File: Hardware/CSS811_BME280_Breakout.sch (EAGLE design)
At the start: 30 parts, among them J1 GATORGATOR_MINI, J2 GATORGATOR_MINI, J3 GATORGATOR_MINI, J4 GATORGATOR_MINI, J5 GATORGATOR_MINI, J6 GATORGATOR_MINI, J7 GATORGATOR_MINI, J8 GATORGATOR_MINI, U2 CCS811, U3 BME280

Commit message: resizing board, adding silk
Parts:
- added LOGO2: SFE_LOGO_NAME_FLAME.1_INCH, SparkFun-Aesthetics:SFE_LOGO_NAME_FLAME.1_INCH
- LOGO1: value SFE_LOGO_NAME.1_INCH -> SFE_LOGO_NAME_FLAME.1_INCH; device SparkFun-Aesthetics:SFE_LOGO_NAME.1_INCH -> SparkFun-Aesthetics:SFE_LOGO_NAME_FLAME.1_INCH
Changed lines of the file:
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@@
 <part name="GND1" library="SparkFun-PowerSymbols" deviceset="GND" device=""/>
 <part name="SUPPLY4" library="SparkFun-PowerSymbols" deviceset="3.3V" device=""/>
-<part name="LOGO1" library="SparkFun-Aesthetics" deviceset="SFE_LOGO_NAME" device=".1_INCH"/>
+<part name="LOGO1" library="SparkFun-Aesthetics" deviceset="SFE_LOGO_NAME_FLAME" device=".1_INCH"/>
 <part name="FD3" library="SparkFun-Aesthetics" deviceset="FIDUCIAL" device="1X2"/>
 <part name="FD4" library="SparkFun-Aesthetics" deviceset="FIDUCIAL" device="1X2"/>
@@
 <part name="J7" library="SparkFun-Connectors" deviceset="GATOR" device="GATOR_MINI"/>
 <part name="J8" library="SparkFun-Connectors" deviceset="GATOR" device="GATOR_MINI"/>
+<part name="LOGO2" library="SparkFun-Aesthetics" deviceset="SFE_LOGO_NAME_FLAME" device=".1_INCH"/>
 </parts>
 <sheets>
@@
 <attribute name="VALUE" x="109.22" y="68.834" size="1.778" layer="96" font="vector" rot="MR0" align="bottom-center"/>
 </instance>
-<instance part="LOGO1" gate="G$1" x="88.9" y="2.54" smashed="yes"/>
+<instance part="LOGO1" gate="G$1" x="91.44" y="2.54" smashed="yes"/>
 <instance part="FD3" gate="G$1" x="241.3" y="27.94" smashed="yes"/>
 <instance part="FD4" gate="G$1" x="241.3" y="25.4" smashed="yes"/>
@@
 <attribute name="NAME" x="119.38" y="60.96" size="1.778" layer="95" font="vector"/>
 </instance>
+<instance part="LOGO2" gate="G$1" x="91.44" y="2.54" smashed="yes"/>
 </instances>
 <busses>

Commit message: finalizing layout/silk
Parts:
- removed ADR1, ADR2: JUMPER-SMT_2_NO_SILK, SparkFun-Jumpers:JUMPER-SMT_2_NO_SILK
- removed JP1: JUMPER-SMT_3_2-NC_TRACE_SILK, SparkFun-Jumpers:JUMPER-SMT_3_2-NC_TRACE_SILK
- LOGO1: value SFE_LOGO_NAME_FLAME.1_INCH -> SFE_LOGO_NAME.1_INCH; device SparkFun-Aesthetics:SFE_LOGO_NAME_FLAME.1_INCH -> SparkFun-Aesthetics:SFE_LOGO_NAME.1_INCH
- R13, R14: value 4.7k -> 10k; device SparkFun-Resistors:4.7KOHM-0603-1/10W-1% -> SparkFun-Resistors:10KOHM-0603-1/10W-1%
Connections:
- removed net N$4: JP1.3, R13.2
- removed net N$5: JP1.1, R14.2
- net 3.3V: now also R13.2, R14.2; no longer JP1.2
- net CCS811_ADDR: no longer ADR1.2
- net GND: no longer ADR1.1, ADR2.1
- net SDO/ADR: no longer ADR2.2
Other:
- note added: "The I2C address of the BME280 is fixed at 0x77"
- note added: "The address of the CCS811 is 0x5B"
- note removed: "ADR1 sets the I2C address of the CCS811. Open (Default) - 0x5B Closed - 0x5A"
- note removed: "ADR2 sets the I2C address of the BME280. Open (Default) - 0x77 Closed - 0x76"
- note removed: "BME280 is configured to I2C mode"
- note removed: "JP1 connects SDA and SCL to 4.7k pull-up resistors."

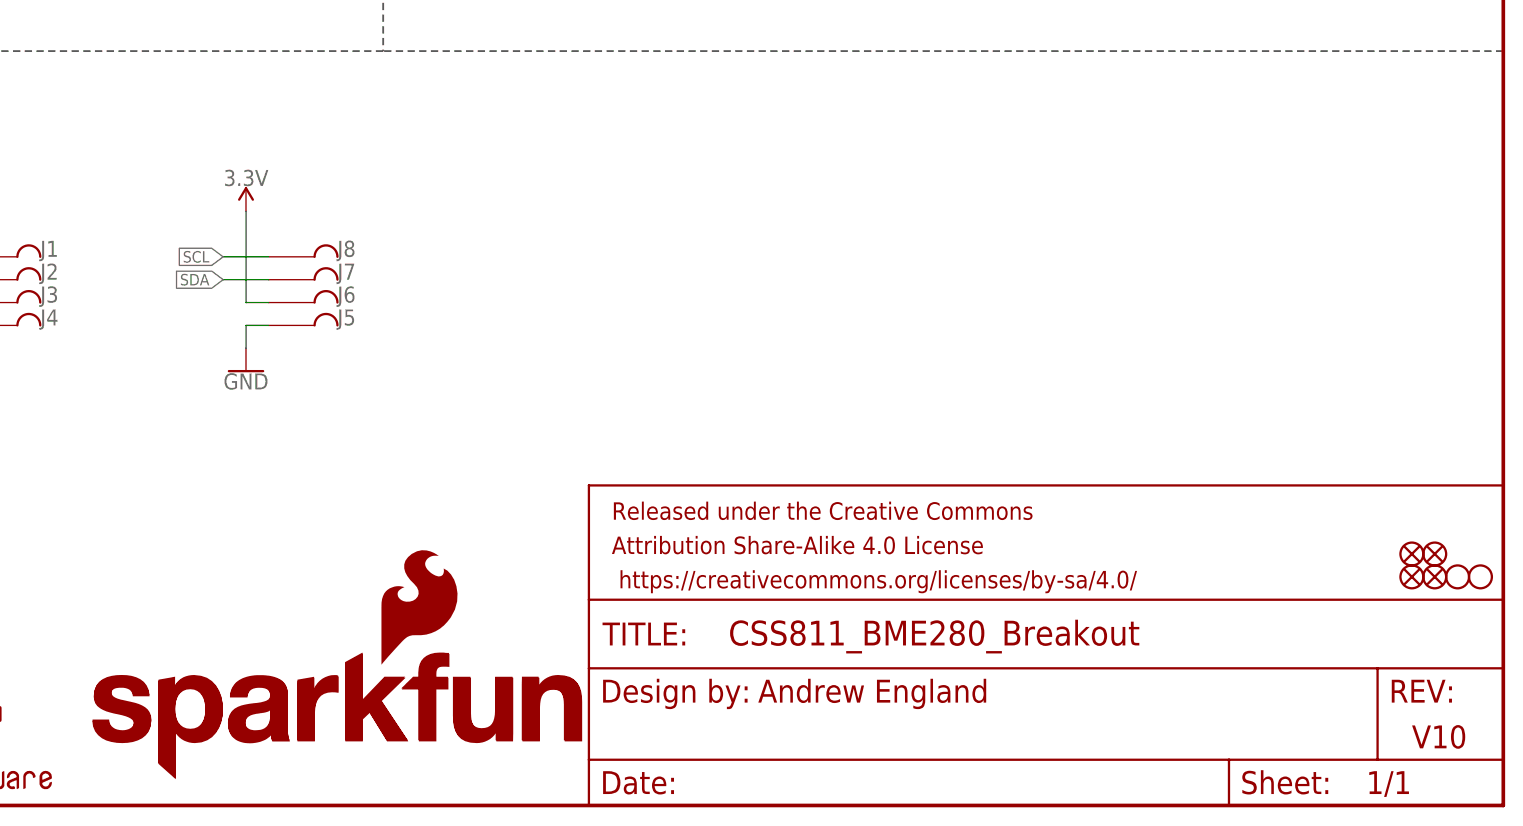
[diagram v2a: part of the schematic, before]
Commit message: adding protection diodes
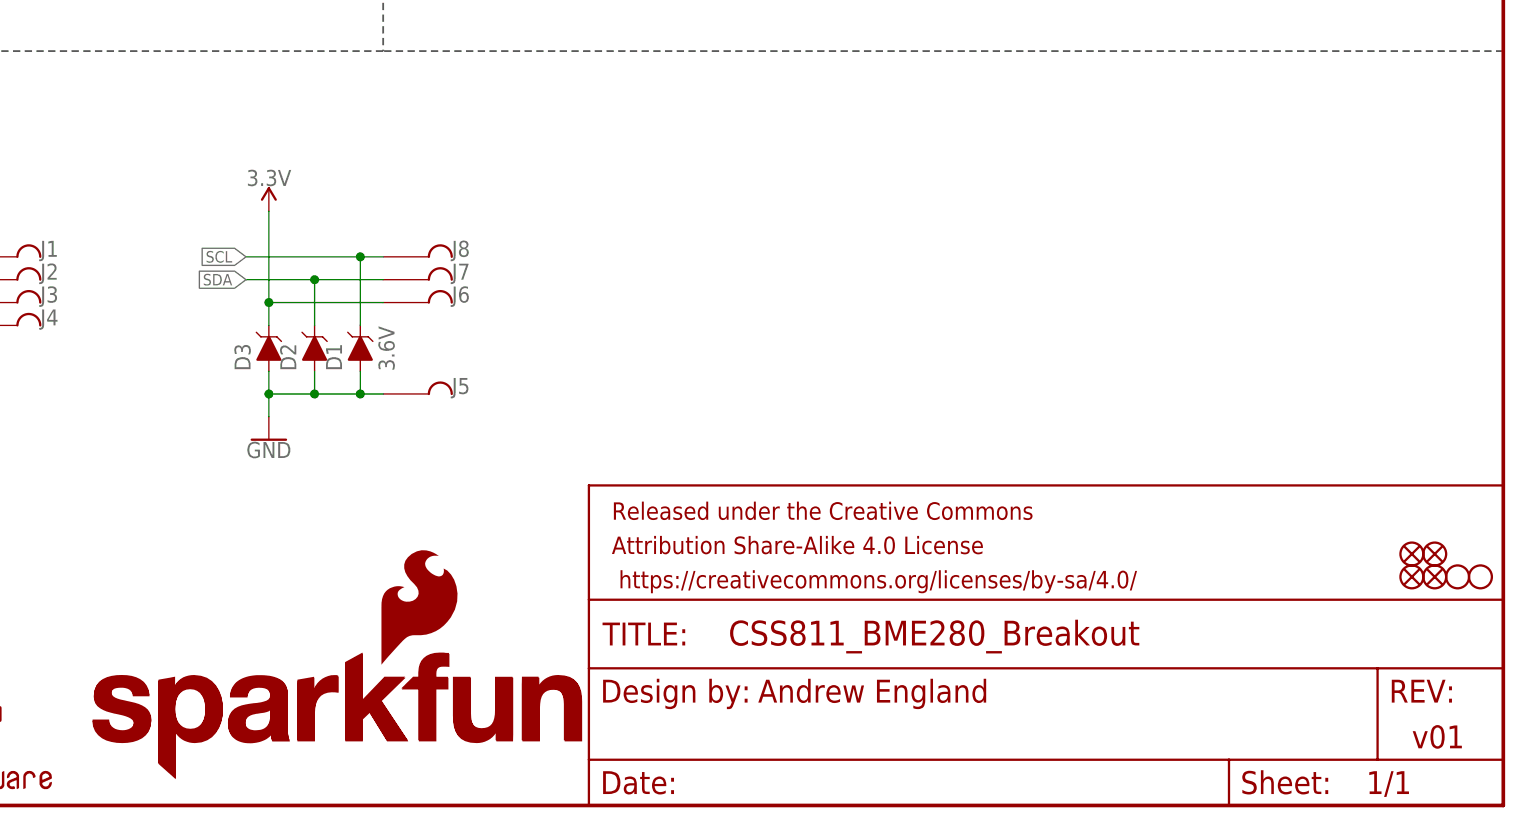
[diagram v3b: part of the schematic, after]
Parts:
- added D1, D2, D3: 3.6V, SparkFun-DiscreteSemi:DIODE-ZENER-BZT52C3V6S
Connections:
- net 3.3V: now also D3.C
- net GND: now also D1.A, D2.A, D3.A
- net SCL: now also D1.C
- net SDA: now also D2.C
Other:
- note added: "v01"
- note removed: "V10"
- moved on the sheet: J5, J6, J7, J8
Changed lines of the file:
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@@
 <?xml version="1.0" encoding="utf-8"?>
 <!DOCTYPE eagle SYSTEM "eagle.dtd">
-<eagle version="9.1.0">
+<eagle version="9.3.1">
 <drawing>
 <settings>
@@
 <part name="J8" library="SparkFun-Connectors" deviceset="GATOR" device="GATOR_MINI"/>
 <part name="LOGO2" library="SparkFun-Aesthetics" deviceset="SFE_LOGO_NAME_FLAME" device=".1_INCH"/>
+<part name="D1" library="SparkFun-DiscreteSemi" deviceset="DIODE-ZENER" device="-BZT52C3V6S" value="3.6V"/>
+<part name="D2" library="SparkFun-DiscreteSemi" deviceset="DIODE-ZENER" device="-BZT52C3V6S" value="3.6V"/>
+<part name="D3" library="SparkFun-DiscreteSemi" deviceset="DIODE-ZENER" device="-BZT52C3V6S" value="3.6V"/>
 </parts>
 <sheets>
@@
 <text x="45.72" y="111.76" size="1.27" layer="97" font="vector" align="center-left">The address of the
 CCS811 is 0x5B</text>
-<text x="238.76" y="7.62" size="2.54" layer="94" font="vector" align="center-left">V10</text>
+<text x="238.76" y="7.62" size="2.54" layer="94" font="vector" align="center-left">v01</text>
 <text x="168.656" y="107.696" size="1.27" layer="97" font="vector" align="top-left">The I2C address
 of the BME280 is
@@
 <attribute name="VALUE" x="71.12" y="103.886" size="1.778" layer="96" font="vector" align="top-center"/>
 </instance>
-<instance part="GND1" gate="1" x="109.22" y="48.26" smashed="yes" rot="MR0">
-<attribute name="VALUE" x="109.22" y="48.006" size="1.778" layer="96" font="vector" rot="MR0" align="top-center"/>
-</instance>
-<instance part="SUPPLY4" gate="G$1" x="109.22" y="66.04" smashed="yes" rot="MR0">
-<attribute name="VALUE" x="109.22" y="68.834" size="1.778" layer="96" font="vector" rot="MR0" align="bottom-center"/>
+<instance part="GND1" gate="1" x="111.76" y="40.64" smashed="yes" rot="MR0">
+<attribute name="VALUE" x="111.76" y="40.386" size="1.778" layer="96" font="vector" rot="MR0" align="top-center"/>
+</instance>
+<instance part="SUPPLY4" gate="G$1" x="111.76" y="66.04" smashed="yes" rot="MR0">
+<attribute name="VALUE" x="111.76" y="68.834" size="1.778" layer="96" font="vector" rot="MR0" align="bottom-center"/>
 </instance>
 <instance part="LOGO1" gate="G$1" x="90.17" y="3.048" smashed="yes"/>
@@
 <attribute name="NAME" x="86.36" y="53.34" size="1.778" layer="95" font="vector"/>
 </instance>
-<instance part="J5" gate="G$1" x="114.3" y="53.34" smashed="yes">
-<attribute name="NAME" x="119.38" y="53.34" size="1.778" layer="95" font="vector"/>
-</instance>
-<instance part="J6" gate="G$1" x="114.3" y="55.88" smashed="yes">
-<attribute name="NAME" x="119.38" y="55.88" size="1.778" layer="95" font="vector"/>
-</instance>
-<instance part="J7" gate="G$1" x="114.3" y="58.42" smashed="yes">
-<attribute name="NAME" x="119.38" y="58.42" size="1.778" layer="95" font="vector"/>
-</instance>
-<instance part="J8" gate="G$1" x="114.3" y="60.96" smashed="yes">
-<attribute name="NAME" x="119.38" y="60.96" size="1.778" layer="95" font="vector"/>
+<instance part="J5" gate="G$1" x="127" y="45.72" smashed="yes">
+<attribute name="NAME" x="132.08" y="45.72" size="1.778" layer="95" font="vector"/>
+</instance>
+<instance part="J6" gate="G$1" x="127" y="55.88" smashed="yes">
+<attribute name="NAME" x="132.08" y="55.88" size="1.778" layer="95" font="vector"/>
+</instance>
+<instance part="J7" gate="G$1" x="127" y="58.42" smashed="yes">
+<attribute name="NAME" x="132.08" y="58.42" size="1.778" layer="95" font="vector"/>
+</instance>
+<instance part="J8" gate="G$1" x="127" y="60.96" smashed="yes">
+<attribute name="NAME" x="132.08" y="60.96" size="1.778" layer="95" font="vector"/>
 </instance>
 <instance part="LOGO2" gate="G$1" x="91.44" y="2.54" smashed="yes"/>
+<instance part="D1" gate="G$1" x="121.92" y="50.8" smashed="yes" rot="R90">
+<attribute name="NAME" x="119.888" y="48.26" size="1.778" layer="95" font="vector" rot="R90"/>
+<attribute name="VALUE" x="123.952" y="48.26" size="1.778" layer="96" font="vector" rot="R90" align="top-left"/>
+</instance>
+<instance part="D2" gate="G$1" x="116.84" y="50.8" smashed="yes" rot="R90">
+<attribute name="NAME" x="114.808" y="48.26" size="1.778" layer="95" font="vector" rot="R90"/>
+</instance>
+<instance part="D3" gate="G$1" x="111.76" y="50.8" smashed="yes" rot="R90">
+<attribute name="NAME" x="109.728" y="48.26" size="1.778" layer="95" font="vector" rot="R90"/>
+</instance>
 </instances>
 <busses>
@@
 </segment>
 <segment>
-<wire x1="111.76" y1="53.34" x2="109.22" y2="53.34" width="0.1524" layer="91"/>
-<wire x1="109.22" y1="53.34" x2="109.22" y2="50.8" width="0.1524" layer="91"/>
+<wire x1="124.46" y1="45.72" x2="121.92" y2="45.72" width="0.1524" layer="91"/>
+<wire x1="121.92" y1="45.72" x2="116.84" y2="45.72" width="0.1524" layer="91"/>
+<wire x1="116.84" y1="45.72" x2="111.76" y2="45.72" width="0.1524" layer="91"/>
+<wire x1="111.76" y1="45.72" x2="111.76" y2="43.18" width="0.1524" layer="91"/>
 <pinref part="GND1" gate="1" pin="GND"/>
 <pinref part="J5" gate="G$1" pin="P$1"/>
+<pinref part="D3" gate="G$1" pin="A"/>
+<wire x1="111.76" y1="45.72" x2="111.76" y2="48.26" width="0.1524" layer="91"/>
+<junction x="111.76" y="45.72"/>
+<pinref part="D2" gate="G$1" pin="A"/>
+<wire x1="116.84" y1="45.72" x2="116.84" y2="48.26" width="0.1524" layer="91"/>
+<junction x="116.84" y="45.72"/>
+<pinref part="D1" gate="G$1" pin="A"/>
+<wire x1="121.92" y1="45.72" x2="121.92" y2="48.26" width="0.1524" layer="91"/>
+<junction x="121.92" y="45.72"/>
 </segment>
 </net>
@@
 </segment>
 <segment>
-<wire x1="111.76" y1="60.96" x2="106.68" y2="60.96" width="0.1524" layer="91"/>
-<label x="106.68" y="60.96" size="1.27" layer="95" font="vector" rot="MR0" xref="yes"/>
+<wire x1="124.46" y1="60.96" x2="121.92" y2="60.96" width="0.1524" layer="91"/>
+<label x="109.22" y="60.96" size="1.27" layer="95" font="vector" rot="MR0" xref="yes"/>
 <pinref part="J8" gate="G$1" pin="P$1"/>
+<pinref part="D1" gate="G$1" pin="C"/>
+<wire x1="121.92" y1="60.96" x2="109.22" y2="60.96" width="0.1524" layer="91"/>
+<wire x1="121.92" y1="60.96" x2="121.92" y2="53.34" width="0.1524" layer="91"/>
+<junction x="121.92" y="60.96"/>
 </segment>
 </net>
@@
 </segment>
 <segment>
-<wire x1="111.76" y1="58.42" x2="106.68" y2="58.42" width="0.1524" layer="91"/>
-<label x="106.68" y="58.42" size="1.27" layer="95" font="vector" rot="MR0" xref="yes"/>
+<wire x1="124.46" y1="58.42" x2="116.84" y2="58.42" width="0.1524" layer="91"/>
+<label x="109.22" y="58.42" size="1.27" layer="95" font="vector" rot="MR0" xref="yes"/>
 <pinref part="J7" gate="G$1" pin="P$1"/>
+<pinref part="D2" gate="G$1" pin="C"/>
+<wire x1="116.84" y1="58.42" x2="109.22" y2="58.42" width="0.1524" layer="91"/>
+<wire x1="116.84" y1="58.42" x2="116.84" y2="53.34" width="0.1524" layer="91"/>
+<junction x="116.84" y="58.42"/>
 </segment>
 </net>
@@
 </segment>
 <segment>
-<wire x1="111.76" y1="55.88" x2="109.22" y2="55.88" width="0.1524" layer="91"/>
-<wire x1="109.22" y1="55.88" x2="109.22" y2="66.04" width="0.1524" layer="91"/>
+<wire x1="124.46" y1="55.88" x2="111.76" y2="55.88" width="0.1524" layer="91"/>
+<wire x1="111.76" y1="55.88" x2="111.76" y2="66.04" width="0.1524" layer="91"/>
 <pinref part="SUPPLY4" gate="G$1" pin="3.3V"/>
 <pinref part="J6" gate="G$1" pin="P$1"/>
+<pinref part="D3" gate="G$1" pin="C"/>
+<wire x1="111.76" y1="55.88" x2="111.76" y2="53.34" width="0.1524" layer="91"/>
+<junction x="111.76" y="55.88"/>
 </segment>
 </net>

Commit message: engineer run of checklist, post review
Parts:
- added D4: RED, SparkFun-LED:LED-RED0603
- added Q1: 2.5A/30V/105mΩ, SparkFun-DiscreteSemi:MOSFET_PCH-DMG2307L
- added R1: 1k, SparkFun-Resistors:1KOHM-0603-1/10W-1%
- added R5: 10k, SparkFun-Resistors:10KOHM-0603-1/10W-1%
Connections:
- new net N$2: D4.A, R1.1
- new net N$3: D3.C, J3.P$1, J6.P$1, Q1.D
- new net N$4: D3.A, Q1.G, R5.2
- net 3.3V: now also Q1.S, R1.2; no longer D3.C, J3.P$1, J6.P$1
- net GND: now also D4.C, R5.1; no longer D3.A
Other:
- note added: "VDD Range: 1.2-3.6V"
- moved on the sheet: D1, D2, D3, J1, J2, J3, J4, J5, J6, J7, J8

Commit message: pushing unsaved changes from checklist
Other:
- moved on the sheet: D1, D2, D3, J1, J2, J3, J4, J5, J6, J7, J8, Q1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
